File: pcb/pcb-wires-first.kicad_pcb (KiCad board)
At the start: 2 copper layers, 110 x 70 mm, 56 parts, among them J1 Conn_01x04, J2 Conn_01x04, J3 Conn_01x04, J4 Conn_01x02, J5 Conn_01x02, J6 Conn_01x02, J7 Conn_01x02, J8 Conn_01x04, SW1 on-1, SW2 off-1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

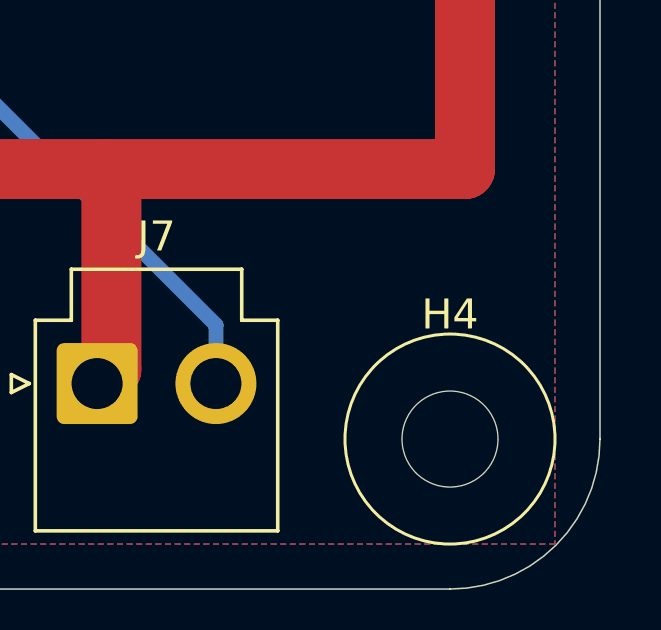
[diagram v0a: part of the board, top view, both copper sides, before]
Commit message: Adding a custom mounting hole footprint which excludes copper.
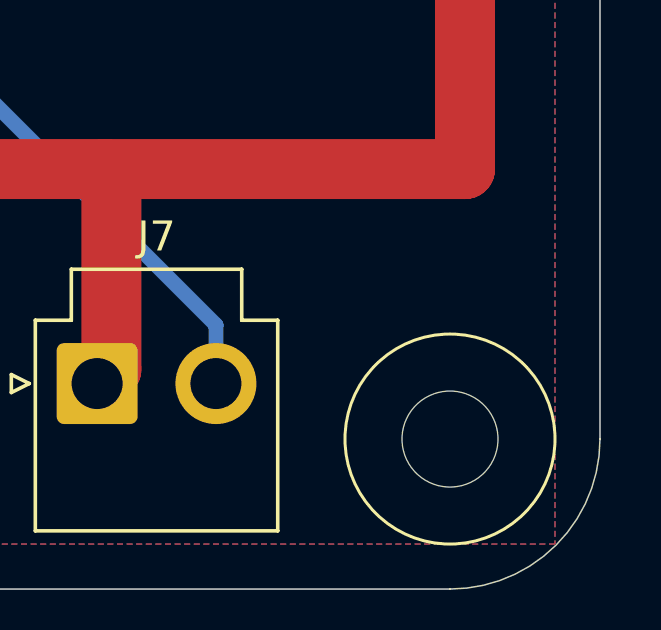
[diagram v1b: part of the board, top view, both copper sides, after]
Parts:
- H1, H2, H3, H4: footprint MountingHole:MountingHole_3.2mm_M3 -> Local:MountingHole_3.2mm_M3

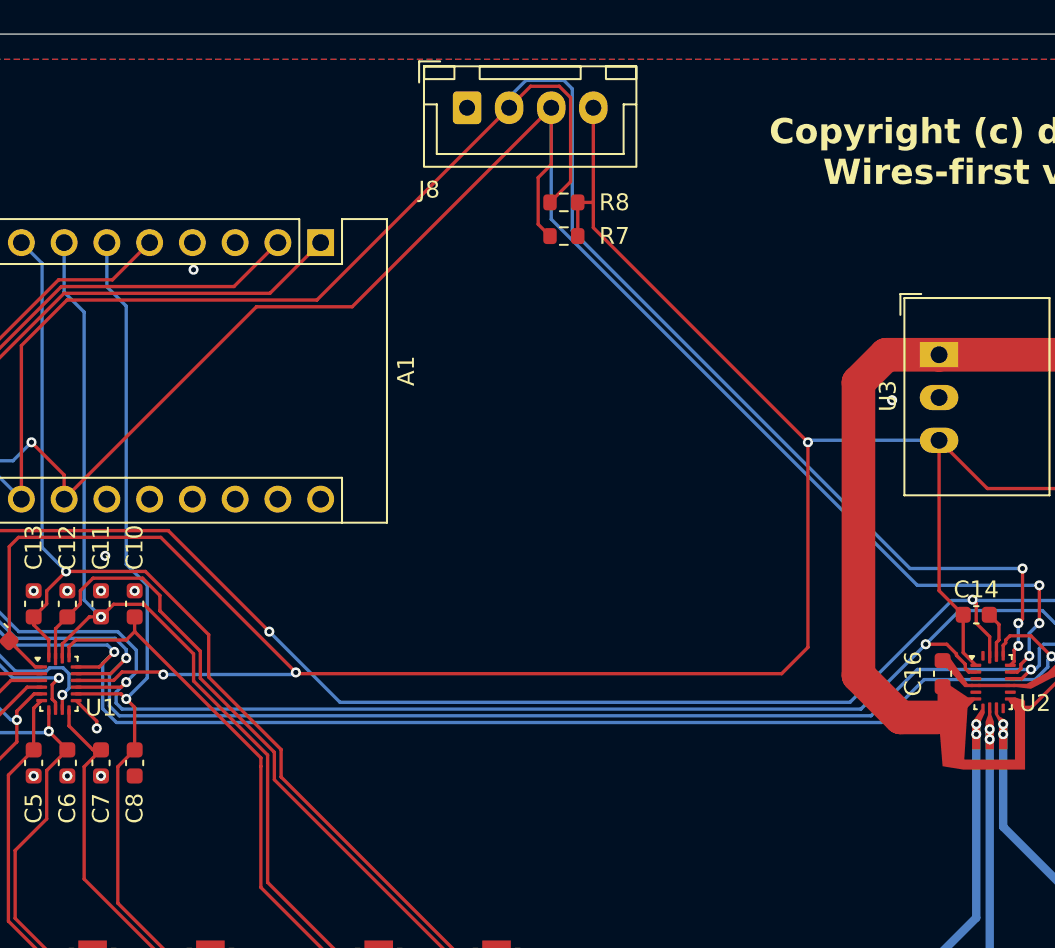
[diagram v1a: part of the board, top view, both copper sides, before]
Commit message: Adding more testpoints.
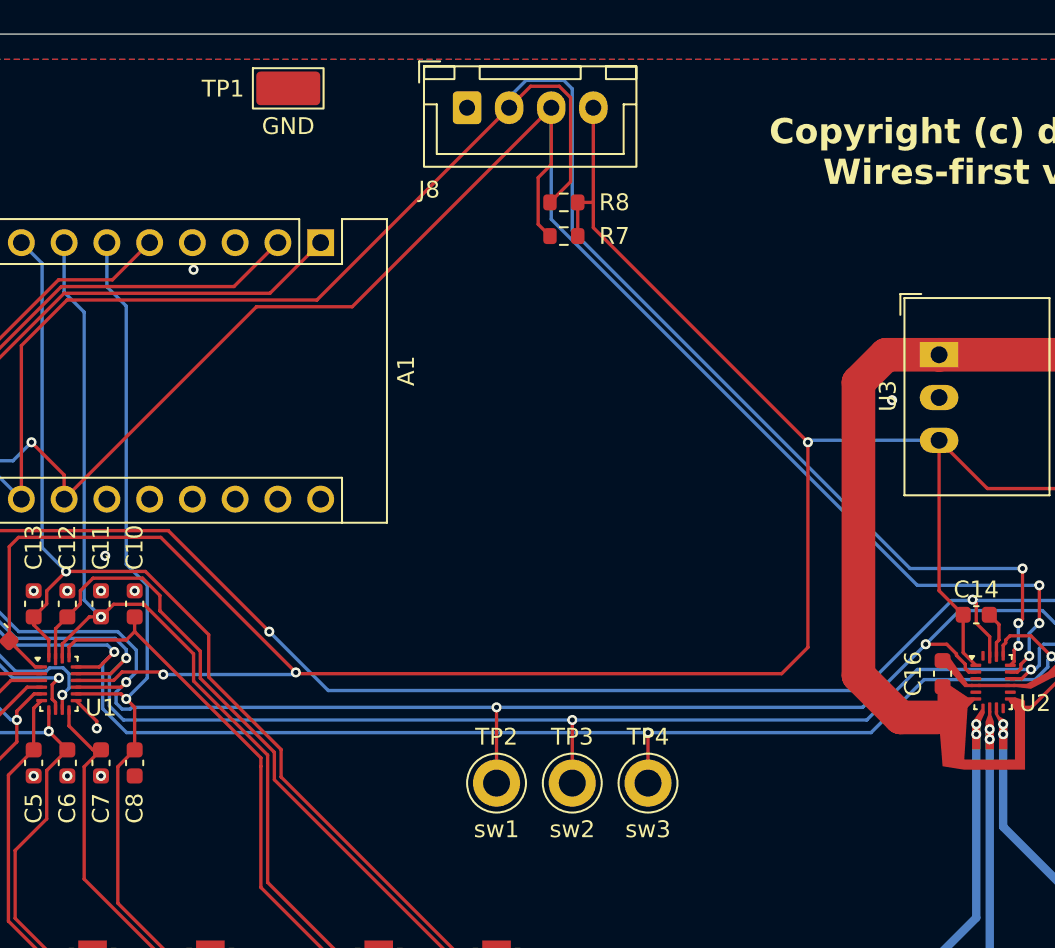
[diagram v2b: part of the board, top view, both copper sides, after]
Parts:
- added TP1: GND, TestPoint:TestPoint_Keystone_5019_Miniature, F.Cu at (100.6, 78.2)
- added TP2: sw1, TestPoint:TestPoint_Keystone_5010-5014_Multipurpose, F.Cu at (113.0, 119.5)
- added TP3: sw2, TestPoint:TestPoint_Keystone_5010-5014_Multipurpose, F.Cu at (117.5, 119.5)
- added TP4: sw3, TestPoint:TestPoint_Keystone_5010-5014_Multipurpose, F.Cu at (122.0, 119.5)
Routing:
- net switch-1: track 97.6 -> 102.1 mm, vias 3 -> 4
- net switch-2: track 96.8 -> 100.8 mm, vias 3 -> 4
- net switch-3: track 101.1 -> 104.6 mm, vias 3 -> 4
- net fault: track 96.3 -> 95.7 mm

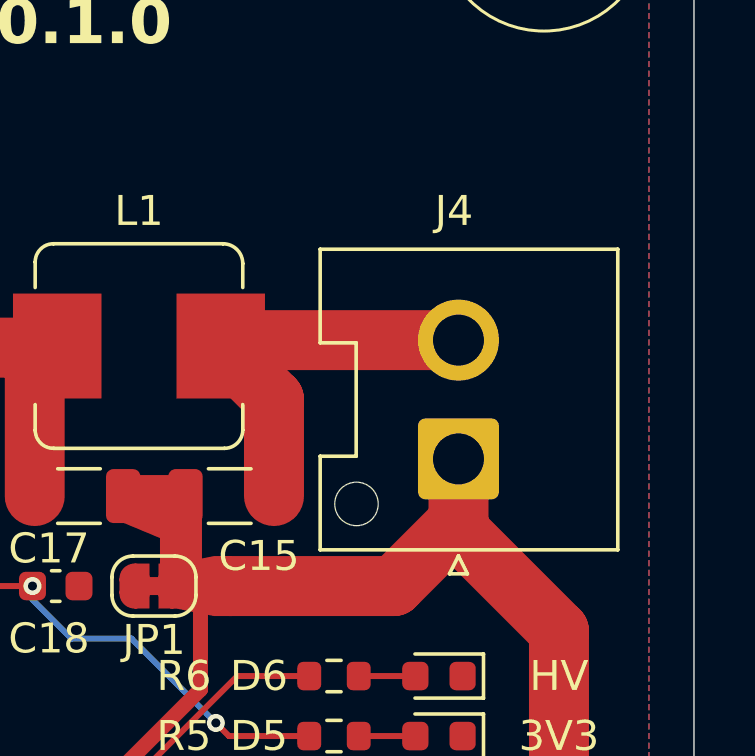
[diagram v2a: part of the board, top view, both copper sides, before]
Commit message: Moving model pusher into a separate project.
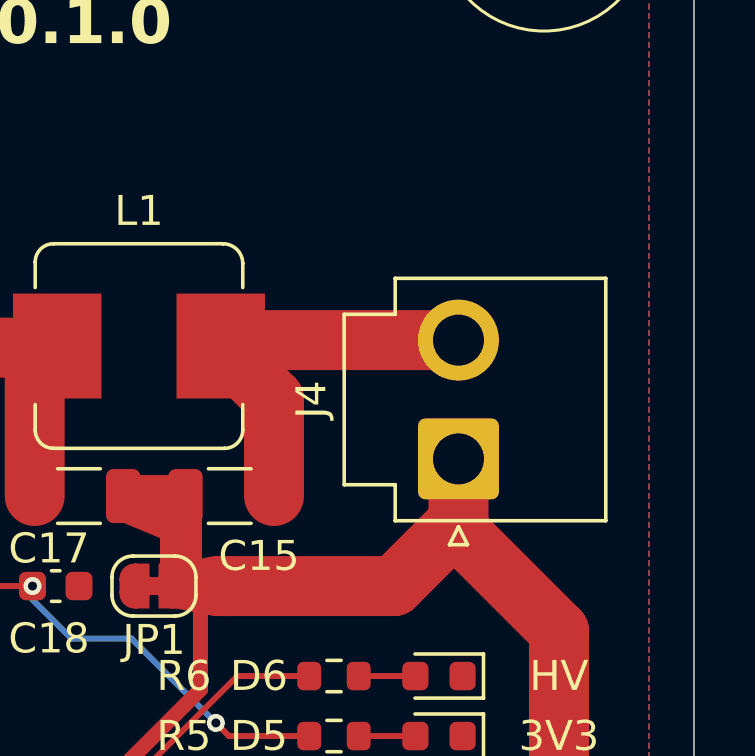
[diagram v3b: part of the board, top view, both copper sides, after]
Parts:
- J4: footprint Connector_JST:JST_VH_B2P-VH-FB-B_1x02_P3.96mm_Vertical -> Connector_JST:JST_VH_B2P-VH_1x02_P3.96mm_Vertical

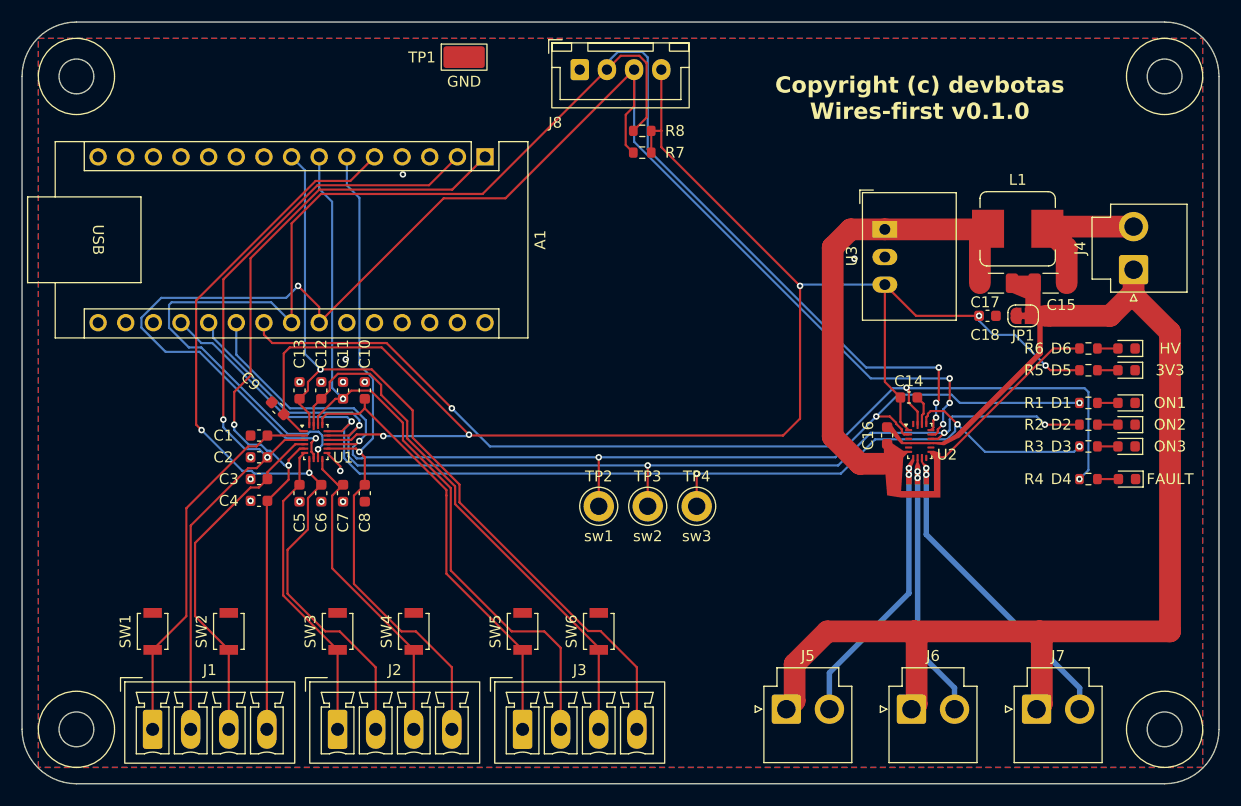
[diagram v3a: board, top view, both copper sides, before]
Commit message: Adjusting tracks.
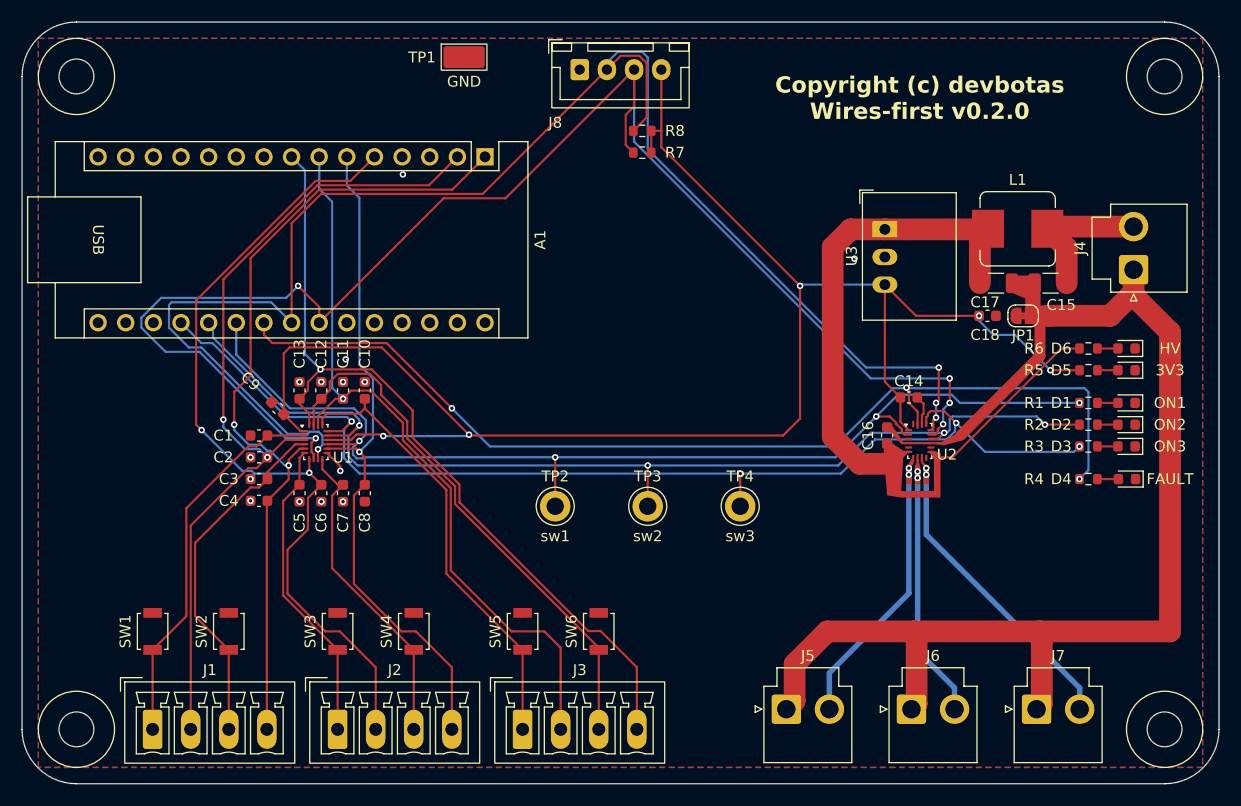
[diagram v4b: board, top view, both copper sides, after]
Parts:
- moved TP2 4.00 mm to (109.0, 119.5)
- moved TP4 4.00 mm to (126.0, 119.5)
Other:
- board text added: "Copyright (c) devbotas Wires-first v0.2.0"
- board text removed: "Copyright (c) devbotas Wires-first v0.1.0"

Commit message: Completely reworking the entire thing. It is sinble-channel now.
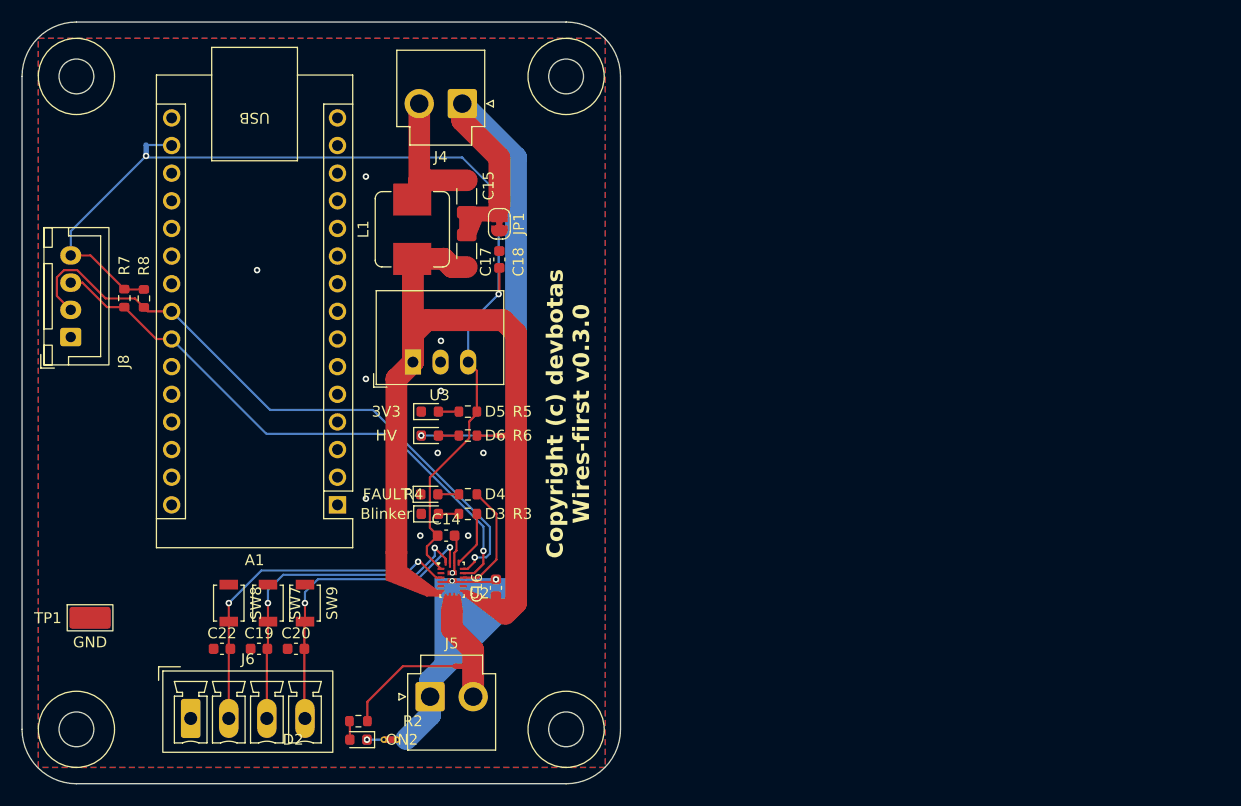
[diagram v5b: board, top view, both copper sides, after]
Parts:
- removed C1, C10, C11, C12, C13, C2, C3, C4, C5, C6, C7, C8, C9: 100nF, Capacitor_SMD:C_0603_1608Metric
- removed D1: ON1, Diode_SMD:D_0603_1608Metric
- removed J1, J2, J3: Conn_01x04, Connector_Phoenix_MC:PhoenixContact_MCV_1,5_4-G-3.5_1x04_P3.50mm_Vertical
- removed J7: Conn_01x02, Connector_JST:JST_VH_B2P-VH_1x02_P3.96mm_Vertical
- removed R1: 2.2k, Resistor_SMD:R_0603_1608Metric
- removed SW1: on-1, Button_Switch_SMD:SW_SPST_B3U-1000P
- removed SW2: off-1, Button_Switch_SMD:SW_SPST_B3U-1000P
- removed SW3: on-2, Button_Switch_SMD:SW_SPST_B3U-1000P
- removed SW4: off-2, Button_Switch_SMD:SW_SPST_B3U-1000P
- removed SW5: on-3, Button_Switch_SMD:SW_SPST_B3U-1000P
- removed SW6: off-3, Button_Switch_SMD:SW_SPST_B3U-1000P
- removed TP2: sw1, TestPoint:TestPoint_Keystone_5010-5014_Multipurpose
- removed TP3: sw2, TestPoint:TestPoint_Keystone_5010-5014_Multipurpose
- removed TP4: sw3, TestPoint:TestPoint_Keystone_5010-5014_Multipurpose
- removed U1: SLG46826V, Package_DFN_QFN:Renesas_UQFN-20_2x3mm_P0.4mm_LayoutBorder4x6y
- added C19: 100nF, Capacitor_SMD:C_0603_1608Metric, F.Cu at (81.8, 132.6)
- added C20: 100nF, Capacitor_SMD:C_0603_1608Metric, F.Cu at (85.2, 132.6)
- added C22: 100nF, Capacitor_SMD:C_0603_1608Metric, F.Cu at (78.4, 132.6)
- added NT1: NetTie_2, NetTie:NetTie-2_SMD_Pad0.5mm, B.Cu at (71.4, 86.8)
- added NT2: NetTie_2, NetTie:NetTie-2_SMD_Pad0.5mm, F.Cu at (104.2, 113.0)
- added NT3: NetTie_2, NetTie:NetTie-2_SMD_Pad0.5mm, B.Cu at (104.2, 113.0)
- added NT4: NetTie_2, NetTie:NetTie-2_SMD_Pad0.5mm, F.Cu at (100.3, 134.2)
- added NT5: NetTie_2, NetTie:NetTie-2_THT_Pad0.3mm, F.Cu at (94.5, 140.9)
- added SW7: set, Button_Switch_SMD:SW_SPST_B3U-1000P, F.Cu at (82.6, 128.4)
- added SW8: reset, Button_Switch_SMD:SW_SPST_B3U-1000P, F.Cu at (79.0, 128.4)
- added SW9: toggle, Button_Switch_SMD:SW_SPST_B3U-1000P, F.Cu at (86.0, 128.4)
- C16: value 100nF -> 1000nF
- D3: value ON3 -> Blinker
- J6: value Conn_01x02 -> Conn_01x04; footprint Connector_JST:JST_VH_B2P-VH_1x02_P3.96mm_Vertical -> Connector_Phoenix_MC:PhoenixContact_MCV_1,5_4-G-3.5_1x04_P3.50mm_Vertical
- R2: value 2.2k -> 6.7k
- moved D2 76.3 mm to (90.9, 140.9)
- moved R2 72.4 mm to (90.9, 139.2), turned to 180 degrees
- moved J6 66.2 mm to (75.5, 139.0)
- moved D6 64.5 mm to (97.5, 113.0), turned to 0 degrees
- moved D3 64.3 mm to (97.5, 120.2), turned to 0 degrees
- moved D5 64.1 mm to (97.5, 110.8), turned to 0 degrees
- moved D4 64.1 mm to (97.4, 118.4), turned to 0 degrees
- moved J4 63.5 mm to (100.5, 82.5), turned to 180 degrees
- moved TP1 61.9 mm to (66.2, 129.8)
- moved R6 57.6 mm to (101.0, 113.0), turned to 180 degrees
- moved R3 57.4 mm to (101.0, 120.2), turned to 180 degrees
- moved R5 57.2 mm to (101.0, 110.8), turned to 180 degrees
- moved R4 57.0 mm to (101.0, 118.4)
- moved L1 55.6 mm to (95.9, 94.0), turned to -90 degrees
- moved H2 55.0 mm to (110.0, 80.0)
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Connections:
- A1 pad 1: /off-1b -> unconnected-(A1-D1/TX-Pad1)
- A1 pad 19: switch-3 -> unconnected-(A1-A0-Pad19)
- A1 pad 2: /on-1b -> unconnected-(A1-D0/RX-Pad2)
- A1 pad 20: switch-2 -> unconnected-(A1-A1-Pad20)
- A1 pad 21: switch-1 -> unconnected-(A1-A2-Pad21)
- A1 pad 22: fault -> unconnected-(A1-A3-Pad22)
- A1 pad 5: /on-2b -> unconnected-(A1-D2-Pad5)
- A1 pad 6: /off-2b -> unconnected-(A1-D3-Pad6)
- A1 pad 7: /on-3b -> unconnected-(A1-D4-Pad7)
- A1 pad 8: /off-3b -> unconnected-(A1-D5-Pad8)
- D2 pad 1: GND -> Net-(D2-K)
- D6 pad 1: GND -> Net-(D6-K)
- J5 pad 2: /output-1 -> /output
- J6 pad 1: HV-GND -> GND
- J6 pad 2: /output-2 -> Net-(J6-Pin_2)
- R2 pad 1: switch-2 -> Net-(NT4-Pad1)
- R3 pad 1: switch-3 -> Net-(U2-GPIO4)
- R4 pad 1: fault -> Net-(D4-A)
- R4 pad 2: Net-(D4-A) -> Net-(U2-GPIO1)
- R6 pad 1: HV-VDD -> Net-(NT2-Pad1)
- U2 pad 10: unconnected-(U2-HV_GPO3-Pad10) -> /output
- U2 pad 14: switch-2 -> Net-(U2-GPIO1)
- U2 pad 17: switch-3 -> Net-(U2-GPIO4)
- U2 pad 19: fault -> Net-(J6-Pin_4)
- U2 pad 2: switch-1 -> unconnected-(U2-GPIO0-Pad2)
- U2 pad 20: unconnected-(U2-GPIO6-Pad20) -> Net-(J6-Pin_3)
- U2 pad 3: unconnected-(U2-GPI-Pad3) -> Net-(J6-Pin_2)
- U2 pad 7: /output-1 -> /output
- U2 pad 8: /output-2 -> /output
- U2 pad 9: /output-3 -> /output
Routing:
- net switch-3: track 104.7 -> 0.00 mm, vias 4 -> 0
- net switch-1: track 102.1 -> 0.00 mm, vias 4 -> 0
- net switch-2: track 100.8 -> 0.00 mm, vias 4 -> 0
- net fault: track 95.7 -> 0.00 mm, vias 3 -> 0
- net SCL: track 140.6 -> 52.8 mm, vias 5 -> 1
- net SDA: track 144.6 -> 59.1 mm, vias 4 -> 1
- net /on-1b: track 77.4 -> 0.00 mm, vias 2 -> 0
- net /on-2b: track 76.3 -> 0.00 mm, vias 2 -> 0
- net /off-1b: track 75.9 -> 0.00 mm, vias 2 -> 0
- net /off-3b: track 75.4 -> 0.00 mm, vias 1 -> 0
- net /on-3b: track 69.9 -> 0.00 mm, vias 1 -> 0
- net /off-2b: track 62.4 -> 0.00 mm, vias 1 -> 0
- net 3V3: track 157.0 -> 95.5 mm, vias 5 -> 2
- net /off-3a: track 50.0 -> 0.00 mm
- net /on-3a: track 41.3 -> 0.00 mm
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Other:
- board size 110 x 70 mm -> 55 x 70 mm
- board text added: "Copyright (c) devbotas Wires-first v0.3.0"
- board text removed: "Copyright (c) devbotas Wires-first v0.2.0"
